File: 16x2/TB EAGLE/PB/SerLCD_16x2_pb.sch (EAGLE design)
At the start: 17 parts, among them J1 AVR_PROG, J3 SER_LCD16X2, U1 5V Flying Jalapeno, U2 74LVC4066_MUX_1:1_X4

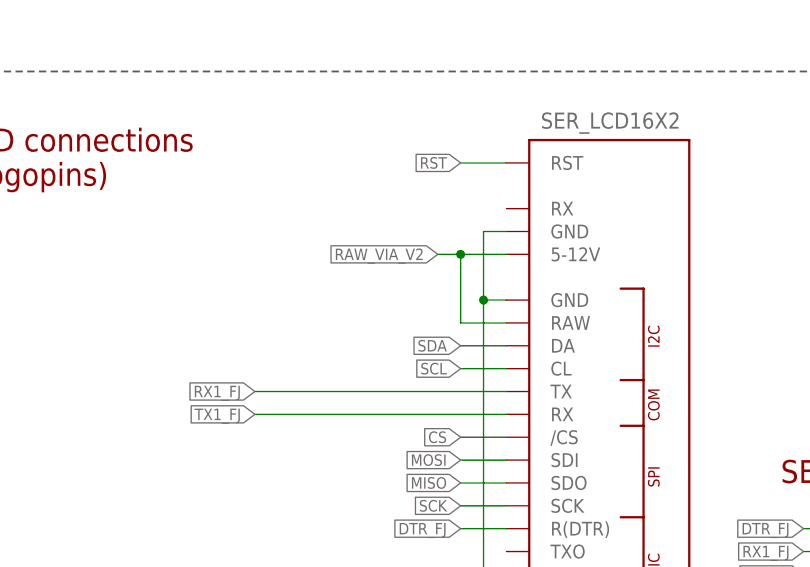
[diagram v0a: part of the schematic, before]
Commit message: 16x2 testbed PB updated for new qwiic connector version
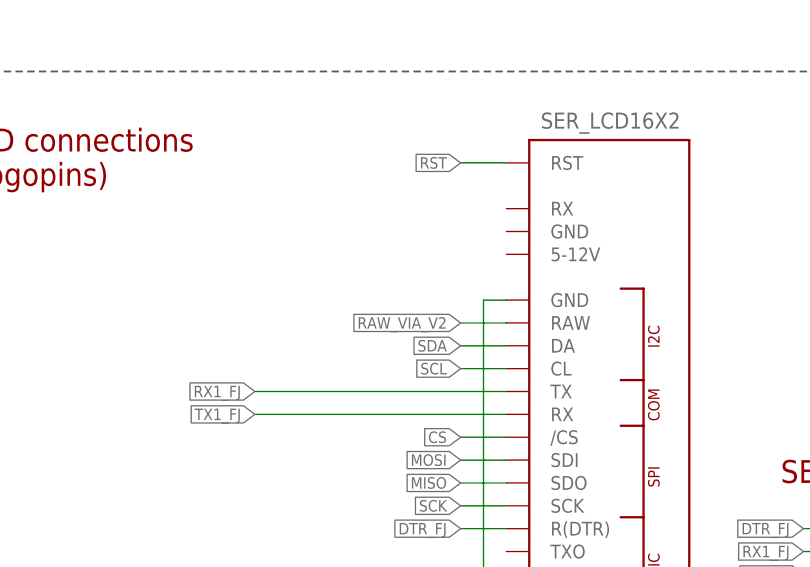
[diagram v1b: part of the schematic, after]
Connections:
- net GND: no longer J3.GND@18
- net RAW_VIA_V2: no longer J3.5-12V
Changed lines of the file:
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@@
 <?xml version="1.0" encoding="utf-8"?>
 <!DOCTYPE eagle SYSTEM "eagle.dtd">
-<eagle version="9.2.2">
+<eagle version="9.5.2">
 <drawing>
 <settings>
@@
 <wire x1="177.8" y1="50.8" x2="175.26" y2="50.8" width="0.1524" layer="91"/>
 <junction x="175.26" y="50.8"/>
-<pinref part="J3" gate="G$1" pin="GND@18"/>
-<wire x1="177.8" y1="93.98" x2="175.26" y2="93.98" width="0.1524" layer="91"/>
-<wire x1="175.26" y1="93.98" x2="175.26" y2="86.36" width="0.1524" layer="91"/>
-<junction x="175.26" y="86.36"/>
 <pinref part="GND5" gate="1" pin="GND"/>
 </segment>
@@
 </segment>
 <segment>
-<pinref part="J3" gate="G$1" pin="5-12V"/>
-<wire x1="177.8" y1="91.44" x2="172.72" y2="91.44" width="0.1524" layer="91"/>
-<label x="170.18" y="91.44" size="1.27" layer="95" rot="R180" xref="yes"/>
+<label x="172.72" y="83.82" size="1.27" layer="95" rot="R180" xref="yes"/>
 <pinref part="J3" gate="G$1" pin="RAW"/>
-<wire x1="172.72" y1="91.44" x2="170.18" y2="91.44" width="0.1524" layer="91"/>
-<wire x1="177.8" y1="83.82" x2="172.72" y2="83.82" width="0.1524" layer="91"/>
-<wire x1="172.72" y1="83.82" x2="172.72" y2="91.44" width="0.1524" layer="91"/>
-<junction x="172.72" y="91.44"/>
-</segment>
-</net>
+<wire x1="172.72" y1="83.82" x2="177.8" y2="83.82" width="0.1524" layer="91"/>
+</segment>
+</net>
